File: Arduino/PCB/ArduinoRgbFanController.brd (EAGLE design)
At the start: 100 x 100 mm, 60 parts, among them IC2 ARDUINO_MKRFOX1200PROTOPADS, Q1 IRLML930, Q2 2N7002, Q3 2N7002, Q4 IRLML930

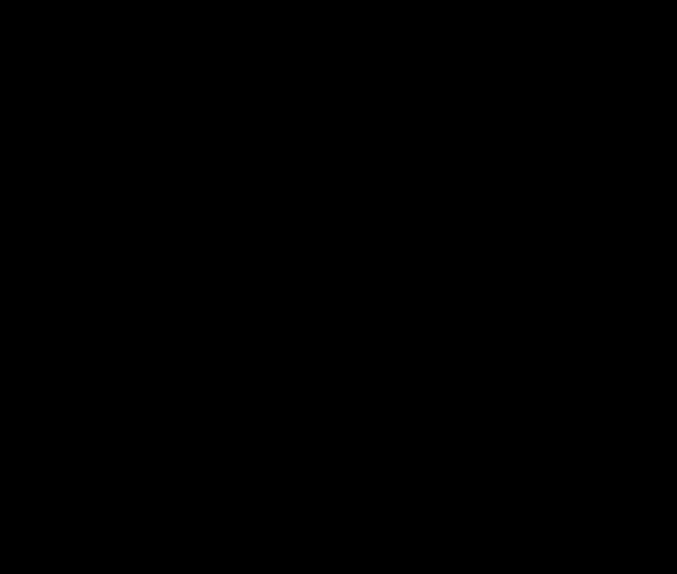
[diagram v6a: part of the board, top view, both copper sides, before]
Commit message: Added required external capacitor and part values.
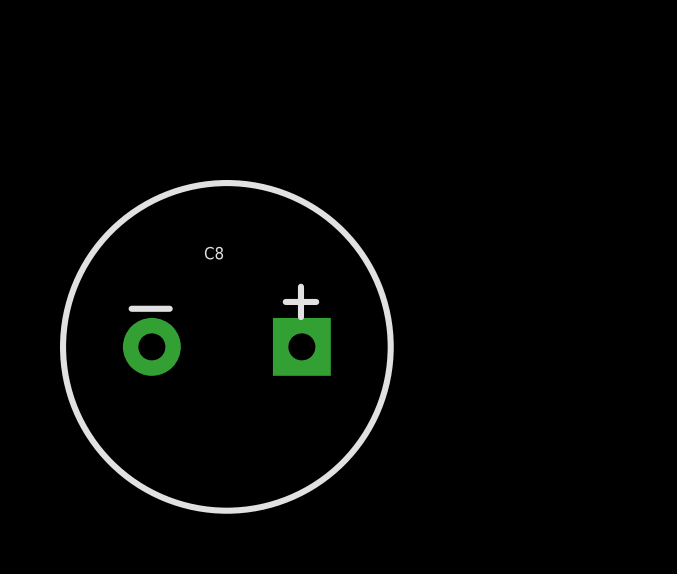
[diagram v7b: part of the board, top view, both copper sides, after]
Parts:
- added C8: 2200uf/16V, SparkFun-Capacitors:CPOL-RADIAL-1000UF-25V-KIT
- C4, C5: value 47uF -> 220uF
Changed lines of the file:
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@@
 <element name="JP15" library="SparkFun-Connectors" package="1X04" value="LED1" x="11.43" y="93.345" smashed="yes">
 <attribute name="VALUE" x="10.16" y="90.17" size="1.27" layer="27"/>
+<attribute name="FARNELL" value="2063775" x="11.43" y="93.345" size="1.778" layer="27" display="off"/>
 </element>
 <element name="JP25" library="SparkFun-Connectors" package="1X04" value="LED2" x="11.43" y="85.725" smashed="yes">
 <attribute name="VALUE" x="10.16" y="82.55" size="1.27" layer="27"/>
+<attribute name="FARNELL" value="2063775" x="11.43" y="85.725" size="1.778" layer="27" display="off"/>
 </element>
 <element name="JP31" library="SparkFun-Connectors" package="1X04" value="LED3" x="11.43" y="78.105" smashed="yes">
 <attribute name="VALUE" x="10.16" y="74.93" size="1.27" layer="27"/>
+<attribute name="FARNELL" value="2063775" x="11.43" y="78.105" size="1.778" layer="27" display="off"/>
 </element>
 <element name="JP34" library="SparkFun-Connectors" package="1X04" value="LED4" x="11.43" y="70.485" smashed="yes">
 <attribute name="VALUE" x="10.16" y="67.31" size="1.27" layer="27"/>
+<attribute name="FARNELL" value="2063775" x="11.43" y="70.485" size="1.778" layer="27" display="off"/>
 </element>
 <element name="JP35" library="SparkFun-Connectors" package="MOLEX-1X3" value="Fan5" x="73.66" y="31.115" smashed="yes"/>
 <element name="JP36" library="SparkFun-Connectors" package="1X04" value="LED5" x="11.43" y="62.865" smashed="yes">
 <attribute name="VALUE" x="10.16" y="59.69" size="1.27" layer="27"/>
+<attribute name="FARNELL" value="2063775" x="11.43" y="62.865" size="1.778" layer="27" display="off"/>
 </element>
 <element name="JP37" library="SparkFun-Connectors" package="1X04" value="LED6" x="11.43" y="55.245" smashed="yes">
 <attribute name="VALUE" x="10.16" y="52.07" size="1.27" layer="27"/>
+<attribute name="FARNELL" value="2063775" x="11.43" y="55.245" size="1.778" layer="27" display="off"/>
 </element>
 <element name="Q1" library="SparkFun-DiscreteSemi" package="SOT23-3" value="IRLML930" x="76.2" y="22.86" smashed="yes">
@@
 <attribute name="VALUE" x="27.178" y="72.4535" size="0.4064" layer="27"/>
 </element>
-<element name="C4" library="SparkFun-Capacitors" package="EIA3528" value="47uF" x="31.75" y="80.645" smashed="yes" rot="R90">
+<element name="C4" library="SparkFun-Capacitors" package="EIA3528" value="220uF" x="31.75" y="80.645" smashed="yes" rot="R90">
 <attribute name="PROD_ID" value="CAP-08310" x="31.75" y="80.645" size="1.778" layer="27" rot="R90" display="off"/>
 <attribute name="NAME" x="33.02" y="84.725" size="1.016" layer="25" rot="R180"/>
 <attribute name="VALUE" x="34.39" y="81.345" size="1.27" layer="27" rot="R180"/>
+<attribute name="FARNELL" value="2491486" x="31.75" y="80.645" size="1.778" layer="27" rot="R90" display="off"/>
 </element>
-<element name="C5" library="SparkFun-Capacitors" package="EIA3528" value="47uF" x="27.94" y="97.155" smashed="yes" rot="R180">
+<element name="C5" library="SparkFun-Capacitors" package="EIA3528" value="220uF" x="27.94" y="97.155" smashed="yes" rot="R180">
 <attribute name="PROD_ID" value="CAP-08310" x="27.94" y="97.155" size="1.778" layer="27" rot="R180" display="off"/>
 <attribute name="NAME" x="31.115" y="95.615" size="1.016" layer="25"/>
 <attribute name="VALUE" x="28.64" y="95.15" size="1.27" layer="27" rot="R90"/>
-<attribute name="FARNELL" value="1135048" x="27.94" y="97.155" size="1.778" layer="27" rot="R180" display="off"/>
+<attribute name="FARNELL" value="2491486" x="27.94" y="97.155" size="1.778" layer="27" rot="R180" display="off"/>
 </element>
 <element name="BME280" library="SparkFun-Connectors" package="1X06" value="eBay BME280" x="41.91" y="24.4475" smashed="yes">
@@
 <attribute name="VALUE" x="13.843" y="47.0535" size="0.4064" layer="27" rot="R270"/>
 </element>
+<element name="C8" library="SparkFun-Capacitors" package="CPOL-RADIAL-1000UF-25V-KIT" value="2200uf/16V" x="-8.5" y="-20.4">
+<attribute name="PROD_ID" value="CAP-09538" x="-8.5" y="-20.4" size="1.778" layer="27" display="off"/>
+</element>
 </elements>
